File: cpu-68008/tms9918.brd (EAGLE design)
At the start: 99.7 x 99.7 mm, 15 parts, among them IC101 GAL22V10D, IC201 74HCT245N

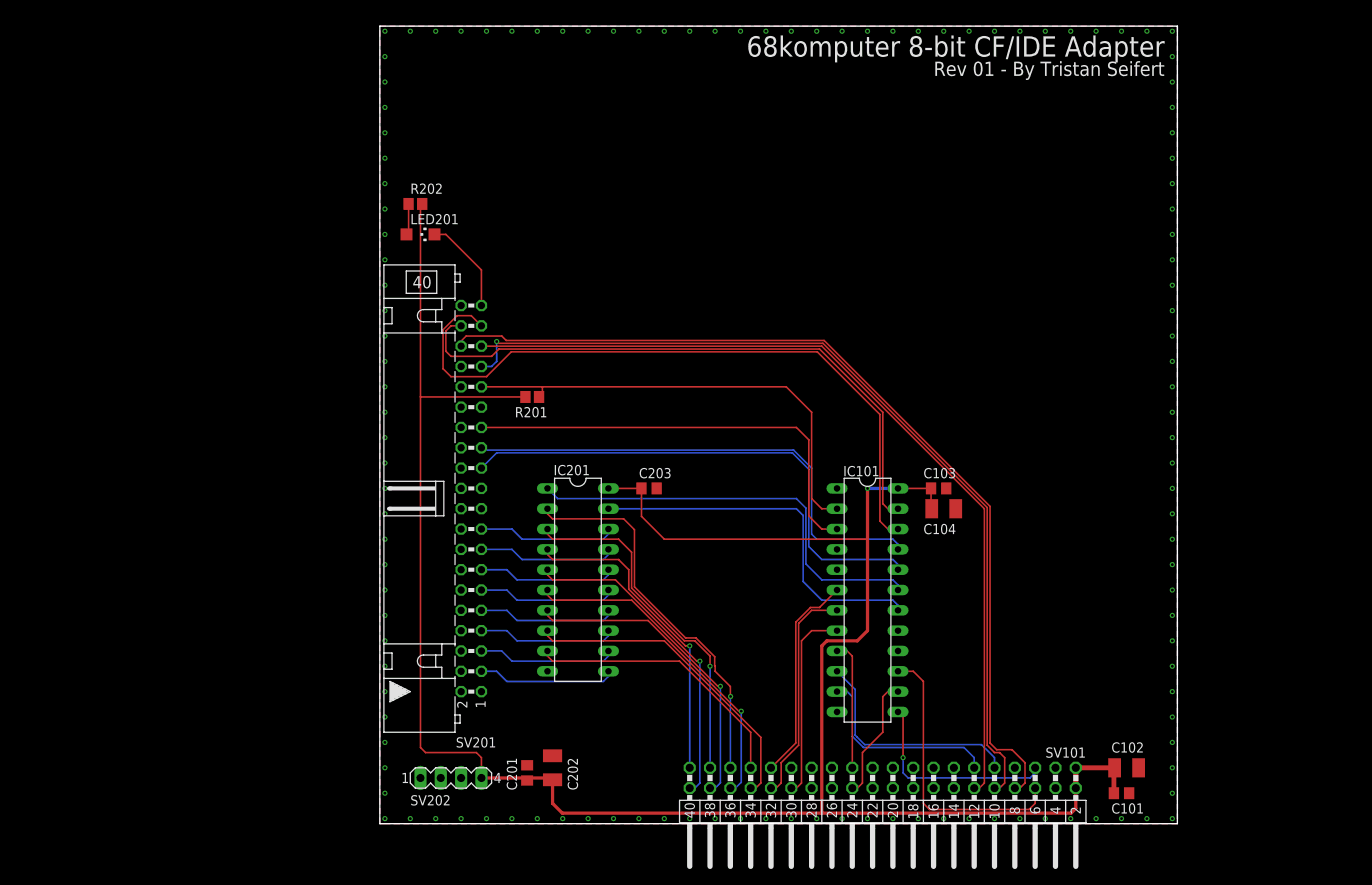
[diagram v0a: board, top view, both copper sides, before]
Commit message: added /DS to GALs on all peripherals and backplane began work on TMS9918 video card
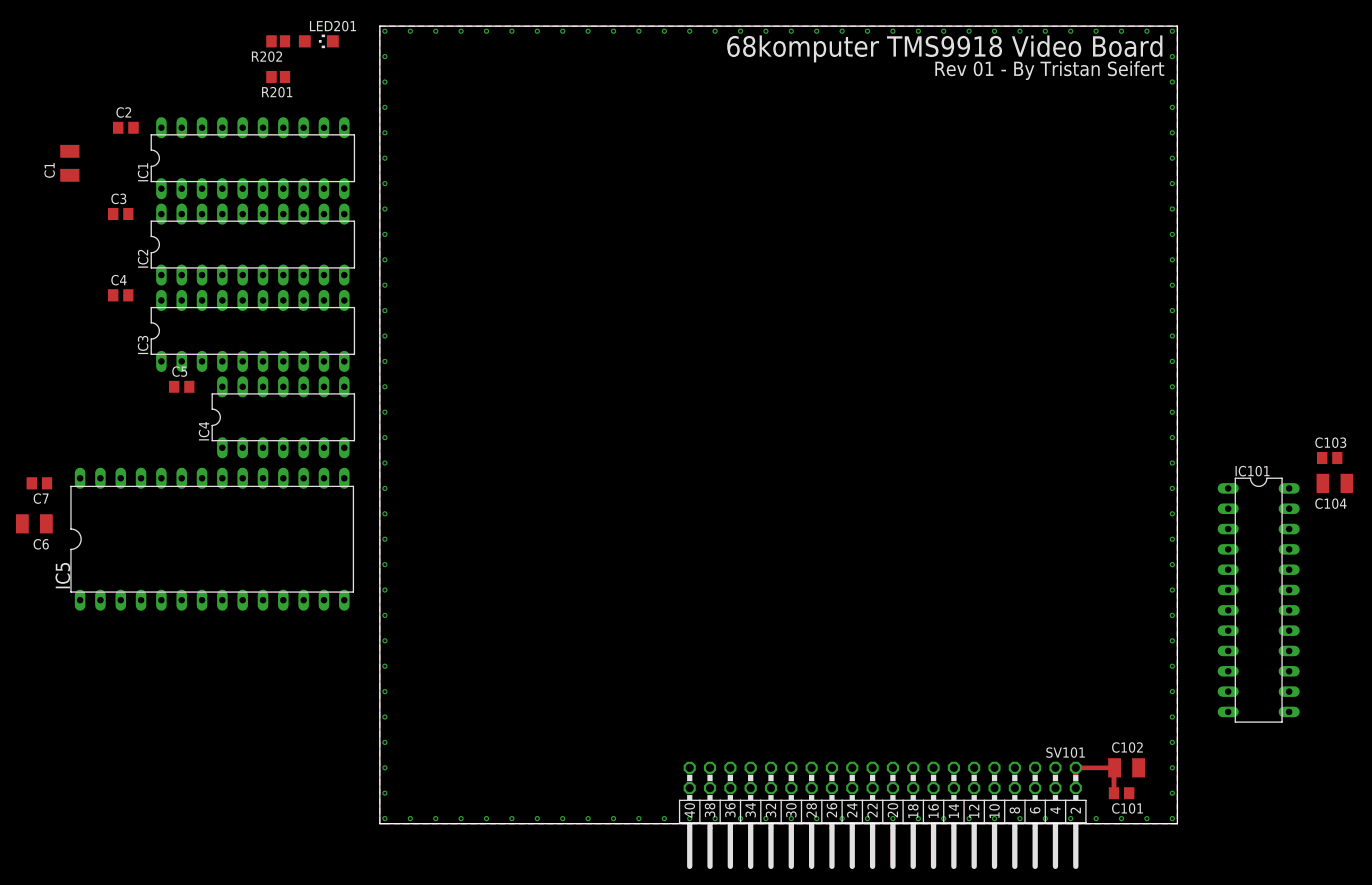
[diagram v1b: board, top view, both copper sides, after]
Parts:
- removed C201, C203: 100nF, rcl:C0805
- removed C202: 10µF, rcl:SMC_B
- removed IC201: 74HCT245N, 74xx-eu:DIL20
- removed SV201: (no value), con-harting-ml:ML40L
- removed SV202: (no value), con-lstb:MA04-1
- added C1, C6: 10µF, rcl:SMC_B
- added C2, C3, C4, C5, C7: 100nF, rcl:C0805
- added IC1, IC2, IC3: 74HCT574N, 74xx-eu:DIL20
- added IC4: 74HCT04N, 74xx-eu:DIL14
- added IC5: AS6C62256, 68komputer:DIL28-6
- moved R201 51.1 mm to (-12.7, 93.3)
- moved C103 49.0 mm to (118.7, 45.7)
- moved C104 49.0 mm to (119.4, 42.5)
- moved IC101 48.9 mm to (109.9, 27.9)
- moved LED201 27.3 mm to (-7.62, 97.8)
- moved R202 26.6 mm to (-12.7, 97.8), turned to 0 degrees
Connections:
- removed net !ATA_BUF_EN: IC101.18, IC201.19
- removed net !ATA_CS0: IC101.22, SV201.37
- removed net !ATA_CS1: IC101.23, SV201.38
- removed net !RESET: SV201.1
- removed net ATA_D0: IC201.18, SV201.17
- removed net ATA_D1: IC201.17, SV201.15
- removed net ATA_D2: IC201.16, SV201.13
- removed net ATA_D3: IC201.15, SV201.11
- removed net ATA_D4: IC201.14, SV201.9
- removed net ATA_D5: IC201.13, SV201.7
- removed net ATA_D6: IC201.12, SV201.5
- removed net ATA_D7: IC201.11, SV201.3
- removed net ATA_DIR: IC101.19, IC201.1
- removed net ATA_IORD: IC101.21, SV201.25
- removed net ATA_IORDY: IC101.3, SV201.27
- removed net ATA_IOWR: IC101.20, SV201.23
- new net !TMS_CAS: IC4.5, IC5.20
- new net !TMS_RAS: IC4.3
- new net !TMS_RD: IC1.11, IC4.13, IC4.2, IC5.22
- new net !TMS_WR: IC4.12
- new net COL: IC3.11, IC4.10
- new net N$1: IC4.11, IC4.8
- new net N$2: IC4.6, IC4.9
- new net ROW: IC2.11, IC4.4
- new net TMS_AD0: IC1.2, IC2.2, IC3.2
- new net TMS_AD1: IC1.3, IC2.3, IC3.3
- new net TMS_AD2: IC1.4, IC2.4, IC3.4
- new net TMS_AD3: IC1.5, IC2.5, IC3.5
- new net TMS_AD4: IC1.6, IC2.6, IC3.6
- new net TMS_AD5: IC1.7, IC2.7, IC3.7
- new net TMS_AD6: IC1.8, IC2.8, IC3.8
- new net TMS_AD7: IC1.9, IC2.9, IC3.9
- new net TMS_R/!W!: IC1.1, IC4.1, IC5.27
- new net TMS_VD0: IC1.19, IC5.11
- new net TMS_VD1: IC1.18, IC5.12
- new net TMS_VD2: IC1.17, IC5.13
- new net TMS_VD3: IC1.16, IC5.15
- new net TMS_VD4: IC1.15, IC5.16
- new net TMS_VD5: IC1.14, IC5.17
- new net TMS_VD6: IC1.13, IC5.18
- new net TMS_VD7: IC1.12, IC5.19
- new net VRAM_A0: IC2.18, IC5.10
- new net VRAM_A1: IC2.17, IC5.9
- new net VRAM_A10: IC3.15, IC5.21
- new net VRAM_A11: IC3.14, IC5.23
- new net VRAM_A12: IC3.13, IC5.2
- new net VRAM_A13: IC3.12, IC5.26
- new net VRAM_A2: IC2.16, IC5.8
- new net VRAM_A3: IC2.15, IC5.7
- new net VRAM_A4: IC2.14, IC5.6
- new net VRAM_A5: IC2.13, IC5.5
- new net VRAM_A6: IC2.12, IC5.4
- new net VRAM_A7: IC3.18, IC5.3
- new net VRAM_A8: IC3.17, IC5.25
- new net VRAM_A9: IC3.16, IC5.24
- new net VRAM_BANK: IC5.1
- net !ATA_ACTY: no longer SV201.39
- net !ATA_IRQ: no longer IC101.2, SV201.31
- net +5V: now also C1.+, C2.1, C3.1, C4.1, C5.1, C6.+, C7.1, IC1.20, IC2.20, IC3.20, IC4.14, IC5.28; no longer C201.1, C202.+, C203.1, IC201.20, SV202.4
- net GND: now also C1.-, C2.2, C3.2, C4.2, C5.2, C6.-, C7.2, IC1.10, IC2.1, IC2.10, IC3.1, IC3.10, IC4.7, IC5.14; no longer C201.2, C202.-, C203.2, IC201.10, SV201.19, SV201.2, SV201.22, SV201.24, SV201.26, SV201.28, SV201.30, SV201.40, SV202.2, SV202.3
- net SLOT_A0: no longer SV201.35
- net SLOT_A1: no longer SV201.33
- net SLOT_A2: no longer SV201.36
- net SLOT_D0: no longer IC201.2
- net SLOT_D1: no longer IC201.3
- net SLOT_D2: no longer IC201.4
- net SLOT_D3: no longer IC201.5
- net SLOT_D4: no longer IC201.6
- net SLOT_D5: no longer IC201.7
- net SLOT_D6: no longer IC201.8
- net SLOT_D7: no longer IC201.9
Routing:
- net +5V: track 276.1 -> 10.6 mm, vias 1 -> 0
- net SLOT_A2: track 114.9 -> 0.00 mm
- net SLOT_A1: track 111.8 -> 0.00 mm, vias 1 -> 0
- net SLOT_A0: track 107.1 -> 0.00 mm
- net !ATA_CS0: track 86.5 -> 0.00 mm
- net !ATA_CS1: track 76.8 -> 0.00 mm
- net ATA_IOWR: track 64.9 -> 0.00 mm
- net ATA_IORD: track 62.5 -> 0.00 mm
- net !ATA_IRQ: track 58.5 -> 0.00 mm
- net ATA_IORDY: track 55.3 -> 0.00 mm
- net ATA_DIR: track 53.5 -> 0.00 mm
- net SLOT_D0: track 47.8 -> 0.00 mm, vias 1 -> 0
- net !ATA_BUF_EN: track 46.7 -> 0.00 mm
- net SLOT_D1: track 43.9 -> 0.00 mm, vias 1 -> 0
- net SLOT_D3: track 40.9 -> 0.00 mm, vias 1 -> 0
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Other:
- board text added: "68komputer TMS9918 Video Board"
- board text removed: "68komputer 8-bit CF/IDE Adapter"

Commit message: finished schematic for tms9918 board, started routing
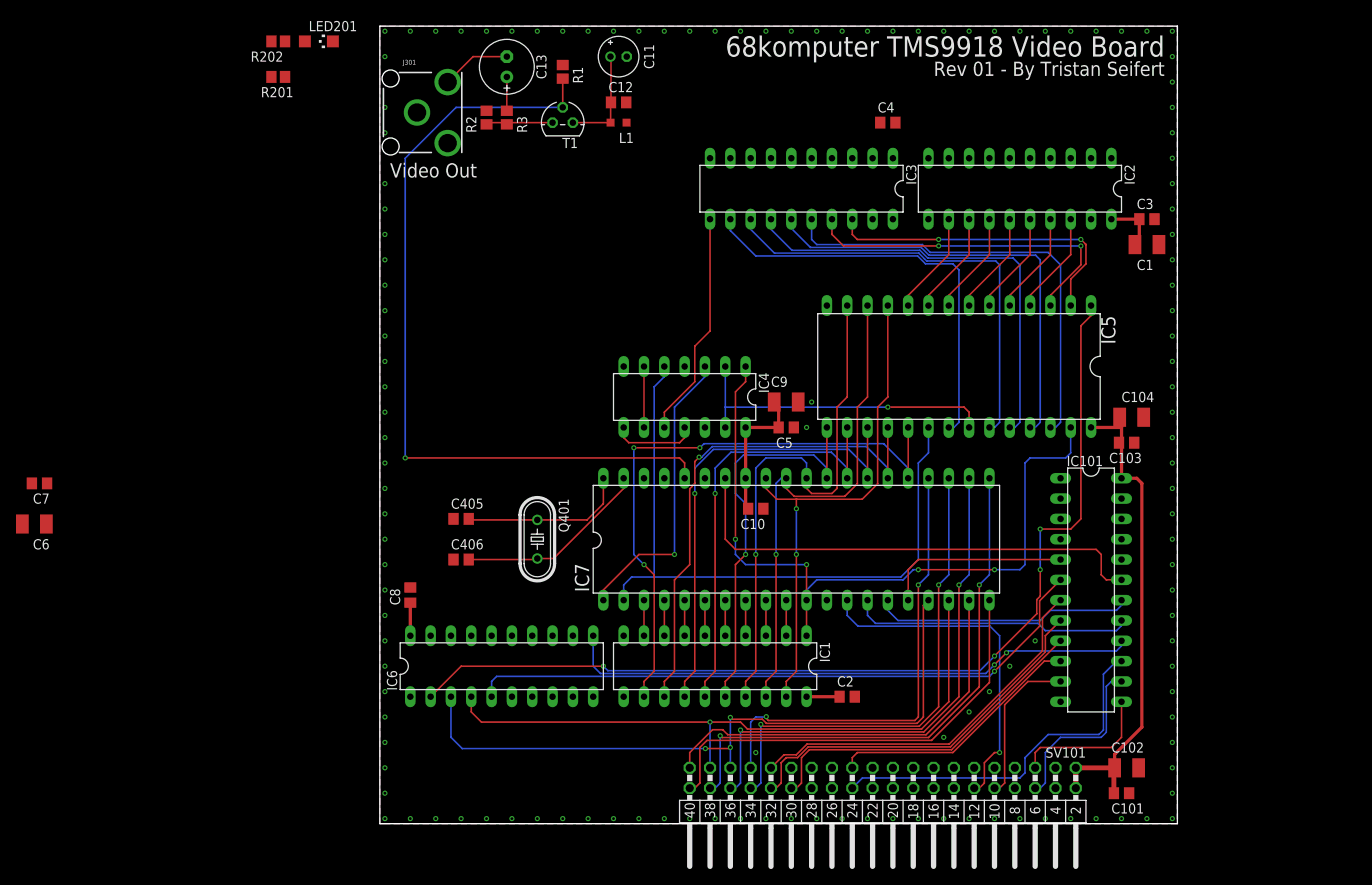
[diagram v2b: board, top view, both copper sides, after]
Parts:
- added C10, C12, C8: 100nF, rcl:C0805
- added C11: 22µF, rcl:E2-5
- added C13: 220µF, rcl:E2,5-7
- added C405, C406: 27pF, rcl:C0805
- added C9: 10µF, rcl:SMC_B
- added IC6: 74HCT373N, 74xx-eu:DIL20
- added IC7: TMS9918, 68komputer:DIL40
- added J301: (no value), SparkFun-Connectors:RCA_LOCK
- added L1: (no value), rcl:L2012C
- added Q401: 10.73866 MHz, crystal:HC49/S
- added R1: 470R, rcl:R2012
- added R2, R3: 75R, rcl:R2012
- added T1: 2N3904, transistor-neu-to92:TO92
- moved C1 135.0 mm to (95.9, 72.4), turned to 0 degrees
- moved C3 128.3 mm to (95.9, 75.6)
- moved C2 114.8 mm to (58.4, 15.9)
- moved C4 98.3 mm to (63.5, 87.6)
- moved IC2 96.1 mm to (80.0, 79.4), turned to 180 degrees
- moved IC5 95.8 mm to (72.4, 57.1), turned to 180 degrees
- moved IC1 85.9 mm to (41.9, 19.7), turned to 180 degrees
- moved C5 75.7 mm to (50.8, 49.5)
- moved IC3 70.8 mm to (52.7, 79.4), turned to 180 degrees
- moved IC4 50.2 mm to (38.1, 53.3), turned to 180 degrees
- moved C104 26.7 mm to (94.0, 50.8)
- moved C103 25.5 mm to (93.3, 47.6)
- moved IC101 21.0 mm to (88.9, 29.2)
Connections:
- removed net !ATA_IRQ: R201.1
- new net !TMS_CS_RD: IC101.18, IC7.15
- new net !TMS_CS_WR: IC101.17, IC7.14
- new net !TMS_IRQ: IC101.5, IC7.16, R201.1
- new net !TMS_RESET: IC101.19, IC7.34
- new net CONFIG_LATCH: IC101.16, IC6.11
- new net N$3: C11.+, C12.1, L1.2, T1.1
- new net N$4: R2.2, R3.2, T1.3
- new net N$5: C13.+, R3.1
- new net N$6: C13.-, J301.PIN
- new net TMS_VID_IN: IC7.35
- new net TMS_VID_OUT: IC7.36, R1.2, T1.2
- new net TMS_X1: C405.2, IC7.40, Q401.1
- new net TMS_X2: C406.2, IC7.39, Q401.2
- new net VDP_RESET: IC101.6, IC6.5
- net !BUS_IRQ: now also IC101.14; no longer IC101.15
- net !SLOT_ACK: now also IC101.15; no longer IC101.14
- net !SLOT_AS: now also IC101.8; no longer IC101.7
- net !SLOT_DS: now also IC101.7; no longer IC101.6
- net !SLOT_RESET: now also IC101.9; no longer IC101.8
- net !TMS_CAS: now also IC7.2
- net !TMS_RAS: now also IC7.1
- net +5V: now also C10.1, C8.1, C9.+, IC6.20, IC7.33, L1.1
- net GND: now also C10.2, C11.-, C12.2, C405.1, C406.1, C8.2, C9.-, IC6.1, IC6.10, IC6.13, IC6.14, IC6.17, IC6.18, IC6.7, IC6.8, IC7.12, J301.SHELL, R1.1, R2.1
- net SLOT_A0: now also IC7.13
- net SLOT_A1: now also IC101.11
- net SLOT_A4: no longer IC101.10
- net SLOT_A5: no longer IC101.11
- net SLOT_D0: now also IC6.3, IC7.17
- net SLOT_D1: now also IC6.4, IC7.18
- net SLOT_D2: now also IC7.19
- net SLOT_D3: now also IC7.20
- net SLOT_D4: now also IC7.21
- net SLOT_D5: now also IC7.22
- net SLOT_D6: now also IC7.23
- net SLOT_D7: now also IC7.24
- net SLOT_R/!W!: now also IC101.10; no longer IC101.9
- net TMS_AD0: now also IC2.9, IC3.9, IC7.10; no longer IC2.2, IC3.2
- net TMS_AD1: now also IC2.8, IC3.8, IC7.9; no longer IC2.3, IC3.3
- net TMS_AD2: now also IC2.7, IC3.7, IC7.8; no longer IC2.4, IC3.4
- net TMS_AD3: now also IC2.6, IC3.6, IC7.7; no longer IC2.5, IC3.5
- net TMS_AD4: now also IC2.5, IC3.5, IC7.6; no longer IC2.6, IC3.6
- net TMS_AD5: now also IC2.4, IC3.4, IC7.5; no longer IC2.7, IC3.7
- net TMS_AD6: now also IC2.3, IC3.3, IC7.4; no longer IC2.8, IC3.8
- net TMS_AD7: now also IC2.2, IC3.2, IC7.3; no longer IC2.9, IC3.9
- net TMS_R/!W!: now also IC7.11
- net TMS_VD0: now also IC7.32
- net TMS_VD1: now also IC7.31
- net TMS_VD2: now also IC7.30
- net TMS_VD3: now also IC7.29
- net TMS_VD4: now also IC7.28
- net TMS_VD5: now also IC7.27
- net TMS_VD6: now also IC7.26
- net TMS_VD7: now also IC7.25
- net VRAM_A0: now also IC2.12; no longer IC2.18
- net VRAM_A1: now also IC2.13; no longer IC2.17
- net VRAM_A10: now also IC3.12; no longer IC3.15
- net VRAM_A11: now also IC3.13; no longer IC3.14
- net VRAM_A12: now also IC3.18; no longer IC3.13
- net VRAM_A13: now also IC3.16; no longer IC3.12
- net VRAM_A2: now also IC2.14; no longer IC2.16
- net VRAM_A4: now also IC2.16; no longer IC2.14
- net VRAM_A5: now also IC2.17; no longer IC2.13
- net VRAM_A6: now also IC2.18; no longer IC2.12
- net VRAM_A7: now also IC3.17; no longer IC3.18
- net VRAM_A8: now also IC3.15; no longer IC3.17
- net VRAM_A9: now also IC3.14; no longer IC3.16
- net VRAM_BANK: now also IC6.2
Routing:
- net VRAM_BANK: track 0.00 -> 124.1 mm, vias 0 -> 4
- net TMS_VID_OUT: track 0.00 -> 100.5 mm, vias 0 -> 1
- net TMS_R/!W!: track 0.00 -> 94.3 mm, vias 0 -> 4
- net SLOT_D0: track 0.00 -> 86.6 mm, vias 0 -> 3
- net +5V: track 10.6 -> 95.1 mm
- net !TMS_CAS: track 0.00 -> 83.9 mm
- net SLOT_D1: track 0.00 -> 82.3 mm, vias 0 -> 1
- net VDP_RESET: track 0.00 -> 80.1 mm, vias 0 -> 1
- net TMS_VD7: track 0.00 -> 76.1 mm, vias 0 -> 3
- net CONFIG_LATCH: track 0.00 -> 72.3 mm, vias 0 -> 2
- net SLOT_D4: track 0.00 -> 69.1 mm, vias 0 -> 2
- net TMS_VD2: track 0.00 -> 67.1 mm, vias 0 -> 1
- net SLOT_D5: track 0.00 -> 65.2 mm, vias 0 -> 2
- net TMS_VD6: track 0.00 -> 64.6 mm, vias 0 -> 1
- net TMS_VD0: track 0.00 -> 64.6 mm, vias 0 -> 2
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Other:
- board text added: "Video Out"
